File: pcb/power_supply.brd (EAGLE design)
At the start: 57.3 x 66.4 mm, 53 parts, among them CON1 +, CON2 +, CON3 +, CON4 +, CON5 +, CON6 +, CON7 +, CON8 +, IC1 AP1507-D5-13, P1 2k, Q1 DIODES_FMMT493ATADIODES_FMMT4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, Q2 DIODES_FMMT493ATADIODES_FMMT4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, Q3 DIODES_FMMT493ATADIODES_FMMT4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, Q4 DIODES_FMMT493ATADIODES_FMMT4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, Q5 DIODES_FMMT493ATADIODES_FMMT4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, Q6 DIODES_FMMT493ATADIODES_FMMT4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, Q7 DIODES_FMMT493ATADIODES_FMMT4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, Q8 DIODES_FMMT493ATADIODES_FMMT4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, U1 LM1085IT-ADJ

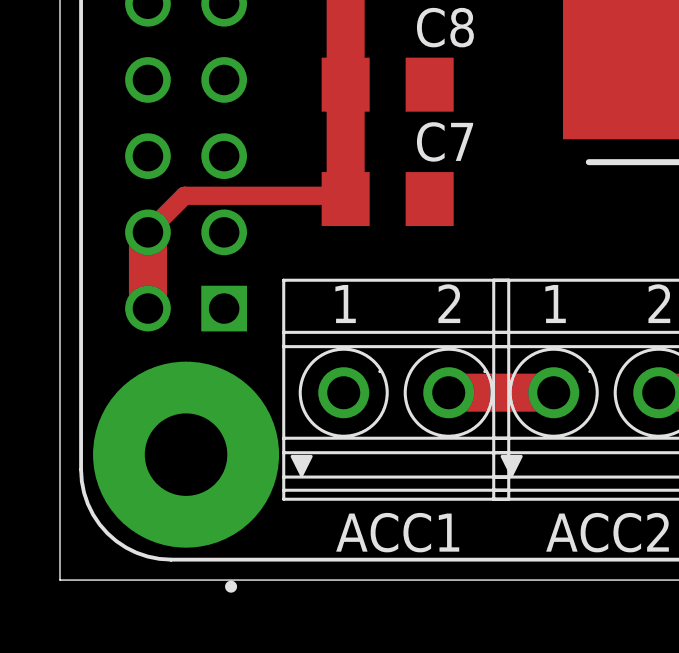
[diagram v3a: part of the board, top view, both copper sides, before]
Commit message: pcb - better supply route
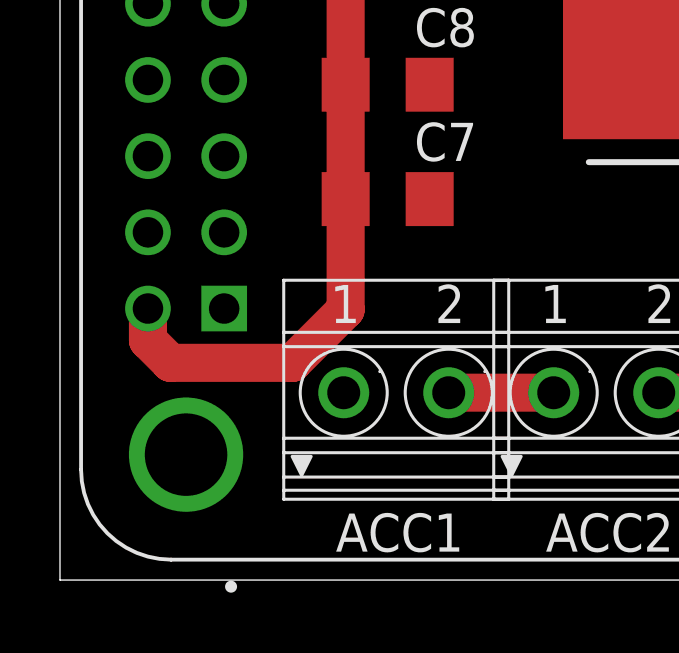
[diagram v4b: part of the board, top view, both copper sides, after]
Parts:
- RASPBERRY: device RASPBERRY_PI_3_MODEL_B_:MODULE_RASPBERRY_PI_3_MODEL_B+ -> RASPBERRY_PI_3_MODEL_B_NoScrew:MODULE_RASPBERRY_PI_3_MODEL_B+
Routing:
- net RASP_SUPPLY: track 34.5 -> 37.2 mm
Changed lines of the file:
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@@
 <attribute name="VALUE" x="18.796" y="48.641" size="1.27" layer="27"/>
 </element>
-<element name="RASPBERRY" library="RASPBERRY_PI_3_MODEL_B_" package="MODULE_RASPBERRY_PI_3_MODEL_B+" value="RASPBERRY_PI_3_MODEL_B+" x="29.21" y="44.45" smashed="yes" rot="R90">
+<element name="RASPBERRY" library="RASPBERRY_PI_3_MODEL_B_NoScrew" package="MODULE_RASPBERRY_PI_3_MODEL_B+" value="RASPBERRY_PI_3_MODEL_B+" x="29.21" y="44.45" smashed="yes" rot="R90">
 <attribute name="AVAILABILITY" value="In Stock" x="60.96" y="102.87" size="1.778" layer="27" rot="R90" display="off"/>
 <attribute name="DESCRIPTION" value=" RASPBERRY PI 3 MOD B+ BCM2837B0 " x="60.96" y="102.87" size="1.778" layer="27" rot="R90" display="off"/>
@@
 <contactref element="RASPBERRY" pad="1"/>
 <contactref element="RASPBERRY" pad="17"/>
-<wire x1="5.98" y1="30.64" x2="5.98" y2="10.32" width="0" layer="19" extent="1-1"/>
+<wire x1="5.98" y1="10.32" x2="5.98" y2="30.64" width="0" layer="19" extent="1-1"/>
 </signal>
 <signal name="GND">
@@
 <contactref element="Q8" pad="2"/>
 <contactref element="ACC1" pad="1"/>
-<wire x1="26.35" y1="27.94" x2="53.71" y2="63.45" width="0" layer="19" extent="1-1"/>
-<wire x1="34.42" y1="20.32" x2="26.35" y2="27.94" width="0" layer="19" extent="1-1"/>
+<wire x1="43.45" y1="58.74" x2="53.71" y2="63.45" width="0" layer="19" extent="1-1"/>
+<wire x1="43.45" y1="52.39" x2="43.45" y2="58.74" width="0" layer="19" extent="1-1"/>
+<wire x1="43.45" y1="46.04" x2="43.45" y2="52.39" width="0" layer="19" extent="1-1"/>
+<wire x1="43.45" y1="39.69" x2="43.45" y2="46.04" width="0" layer="19" extent="1-1"/>
+<wire x1="43.45" y1="33.34" x2="43.45" y2="39.69" width="0" layer="19" extent="1-1"/>
+<wire x1="43.45" y1="26.99" x2="43.45" y2="33.34" width="0" layer="19" extent="1-1"/>
+<wire x1="39.37" y1="22.86" x2="43.45" y2="26.99" width="0" layer="19" extent="1-1"/>
+<wire x1="34.42" y1="20.32" x2="39.37" y2="22.86" width="0" layer="19" extent="1-1"/>
 <wire x1="34.42" y1="16.51" x2="34.42" y2="20.32" width="0" layer="19" extent="1-1"/>
-<wire x1="32.854" y1="8.89" x2="34.42" y2="16.51" width="0" layer="19" extent="1-1"/>
-<wire x1="32.854" y1="12.7" x2="32.854" y2="8.89" width="0" layer="19" extent="1-1"/>
-<wire x1="39.37" y1="22.86" x2="32.854" y2="12.7" width="0" layer="19" extent="1-1"/>
-<wire x1="20.14" y1="19.05" x2="32.854" y2="8.89" width="0" layer="19" extent="1-1"/>
-<wire x1="26.885" y1="19.05" x2="20.14" y2="19.05" width="0" layer="19" extent="1-1"/>
-<wire x1="26.885" y1="21.59" x2="26.885" y2="19.05" width="0" layer="19" extent="1-1"/>
-<wire x1="5.98" y1="40.8" x2="26.885" y2="21.59" width="0" layer="19" extent="1-1"/>
+<wire x1="32.854" y1="12.7" x2="34.42" y2="16.51" width="0" layer="19" extent="1-1"/>
+<wire x1="32.854" y1="8.89" x2="32.854" y2="12.7" width="0" layer="19" extent="1-1"/>
+<wire x1="33.02" y1="25.72" x2="34.42" y2="20.32" width="0" layer="19" extent="1-1"/>
+<wire x1="33.02" y1="32.07" x2="33.02" y2="25.72" width="0" layer="19" extent="1-1"/>
+<wire x1="33.02" y1="38.42" x2="33.02" y2="32.07" width="0" layer="19" extent="1-1"/>
+<wire x1="33.02" y1="44.77" x2="33.02" y2="38.42" width="0" layer="19" extent="1-1"/>
+<wire x1="33.02" y1="51.12" x2="33.02" y2="44.77" width="0" layer="19" extent="1-1"/>
+<wire x1="33.02" y1="57.47" x2="33.02" y2="51.12" width="0" layer="19" extent="1-1"/>
+<wire x1="26.35" y1="27.94" x2="33.02" y2="25.72" width="0" layer="19" extent="1-1"/>
+<wire x1="26.885" y1="21.59" x2="26.35" y2="27.94" width="0" layer="19" extent="1-1"/>
+<wire x1="26.885" y1="19.05" x2="26.885" y2="21.59" width="0" layer="19" extent="1-1"/>
+<wire x1="20.14" y1="19.05" x2="26.885" y2="19.05" width="0" layer="19" extent="1-1"/>
+<wire x1="12.83" y1="17.78" x2="20.14" y2="19.05" width="0" layer="19" extent="1-1"/>
+<wire x1="12.83" y1="13.97" x2="12.83" y2="17.78" width="0" layer="19" extent="1-1"/>
+<wire x1="9.9657" y1="7.5138" x2="12.83" y2="13.97" width="0" layer="19" extent="1-1"/>
+<wire x1="4.71" y1="5.45" x2="9.9657" y2="7.5138" width="0" layer="19" extent="1-1"/>
+<wire x1="5.98" y1="20.48" x2="12.83" y2="17.78" width="0" layer="19" extent="1-1"/>
+<wire x1="3.44" y1="25.56" x2="5.98" y2="20.48" width="0" layer="19" extent="1-1"/>
+<wire x1="3.44" y1="15.4" x2="5.98" y2="20.48" width="0" layer="19" extent="1-1"/>
+<wire x1="25.67" y1="56.2" x2="33.02" y2="57.47" width="0" layer="19" extent="1-1"/>
+<wire x1="25.67" y1="49.85" x2="25.67" y2="56.2" width="0" layer="19" extent="1-1"/>
+<wire x1="3.44" y1="33.18" x2="3.44" y2="25.56" width="0" layer="19" extent="1-1"/>
+<wire x1="38.7985" y1="3.8471" x2="32.854" y2="8.89" width="0" layer="19" extent="1-1"/>
+<wire x1="25.4" y1="40.3" x2="33.02" y2="38.42" width="0" layer="19" extent="1-1"/>
+<wire x1="5.98" y1="40.8" x2="3.44" y2="33.18" width="0" layer="19" extent="1-1"/>
 <wire x1="3.44" y1="45.88" x2="5.98" y2="40.8" width="0" layer="19" extent="1-1"/>
 <wire x1="3.44" y1="50.96" x2="3.44" y2="45.88" width="0" layer="19" extent="1-1"/>
 <wire x1="5.98" y1="58.58" x2="3.44" y2="50.96" width="0" layer="19" extent="1-1"/>
 <wire x1="4.71" y1="63.45" x2="5.98" y2="58.58" width="0" layer="19" extent="1-1"/>
-<wire x1="3.44" y1="33.18" x2="5.98" y2="40.8" width="0" layer="19" extent="1-1"/>
-<wire x1="3.44" y1="25.56" x2="3.44" y2="33.18" width="0" layer="19" extent="1-1"/>
-<wire x1="5.98" y1="20.48" x2="3.44" y2="25.56" width="0" layer="19" extent="1-1"/>
-<wire x1="25.4" y1="40.3" x2="5.98" y2="20.48" width="0" layer="19" extent="1-1"/>
-<wire x1="3.44" y1="15.4" x2="5.98" y2="20.48" width="0" layer="19" extent="1-1"/>
-<wire x1="12.83" y1="13.97" x2="3.44" y2="15.4" width="0" layer="19" extent="1-1"/>
-<wire x1="12.83" y1="17.78" x2="12.83" y2="13.97" width="0" layer="19" extent="1-1"/>
-<wire x1="9.9657" y1="7.5138" x2="12.83" y2="13.97" width="0" layer="19" extent="1-1"/>
-<wire x1="4.71" y1="5.45" x2="9.9657" y2="7.5138" width="0" layer="19" extent="1-1"/>
-<wire x1="53.595" y1="11.43" x2="39.37" y2="22.86" width="0" layer="19" extent="1-1"/>
-<wire x1="53.71" y1="5.45" x2="53.595" y2="11.43" width="0" layer="19" extent="1-1"/>
-<wire x1="38.7985" y1="3.8471" x2="53.595" y2="11.43" width="0" layer="19" extent="1-1"/>
-<wire x1="33.02" y1="25.72" x2="4.71" y2="63.45" width="0" layer="19" extent="1-1"/>
-<wire x1="33.02" y1="32.07" x2="33.02" y2="25.72" width="0" layer="19" extent="1-1"/>
-<wire x1="33.02" y1="38.42" x2="33.02" y2="32.07" width="0" layer="19" extent="1-1"/>
-<wire x1="33.02" y1="44.77" x2="33.02" y2="38.42" width="0" layer="19" extent="1-1"/>
-<wire x1="43.45" y1="26.99" x2="33.02" y2="44.77" width="0" layer="19" extent="1-1"/>
-<wire x1="43.45" y1="33.34" x2="43.45" y2="26.99" width="0" layer="19" extent="1-1"/>
-<wire x1="43.45" y1="39.69" x2="43.45" y2="33.34" width="0" layer="19" extent="1-1"/>
-<wire x1="43.45" y1="46.04" x2="43.45" y2="39.69" width="0" layer="19" extent="1-1"/>
-<wire x1="25.67" y1="49.85" x2="43.45" y2="46.04" width="0" layer="19" extent="1-1"/>
-<wire x1="43.45" y1="52.39" x2="25.67" y2="49.85" width="0" layer="19" extent="1-1"/>
-<wire x1="25.67" y1="56.2" x2="43.45" y2="52.39" width="0" layer="19" extent="1-1"/>
-<wire x1="43.45" y1="58.74" x2="25.67" y2="56.2" width="0" layer="19" extent="1-1"/>
-<wire x1="15.24" y1="48.58" x2="25.67" y2="49.85" width="0" layer="19" extent="1-1"/>
-<wire x1="33.02" y1="51.12" x2="25.67" y2="56.2" width="0" layer="19" extent="1-1"/>
-<wire x1="33.02" y1="57.47" x2="43.45" y2="58.74" width="0" layer="19" extent="1-1"/>
+<wire x1="15.24" y1="54.93" x2="5.98" y2="58.58" width="0" layer="19" extent="1-1"/>
+<wire x1="15.24" y1="48.58" x2="15.24" y2="54.93" width="0" layer="19" extent="1-1"/>
+<wire x1="53.71" y1="5.45" x2="38.7985" y2="3.8471" width="0" layer="19" extent="1-1"/>
+<wire x1="53.595" y1="11.43" x2="53.71" y2="5.45" width="0" layer="19" extent="1-1"/>
 </signal>
 <signal name="BAT">
@@
 <wire x1="19.2608" y1="57.2592" x2="19.37" y2="57.15" width="0.6096" layer="1"/>
 <wire x1="4.6592" y1="57.2592" x2="19.2608" y2="57.2592" width="0.6096" layer="1"/>
-<wire x1="15.24" y1="56.83" x2="19.37" y2="57.15" width="0" layer="19" extent="1-1"/>
+<wire x1="19.37" y1="57.15" x2="15.56" y2="57.15" width="0" layer="19" extent="1-1"/>
 </signal>
 <signal name="N$27">
@@
 <wire x1="10.03" y1="37.55" x2="10.03" y2="13.97" width="1.27" layer="1"/>
 <wire x1="10.03" y1="13.97" x2="10.03" y2="14.0792" width="0.6096" layer="1"/>
-<wire x1="10.03" y1="14.0792" x2="4.6592" y2="14.0792" width="0.6096" layer="1"/>
-<wire x1="4.6592" y1="14.0792" x2="3.44" y2="12.86" width="0.6096" layer="1"/>
 <wire x1="3.80941875" y1="10.32" x2="3.44" y2="10.32" width="0.6096" layer="1"/>
-<wire x1="3.44" y1="12.86" x2="3.44" y2="10.32" width="1.27" layer="1"/>
+<wire x1="3.44" y1="10.32" x2="3.44" y2="9.26" width="1.27" layer="1"/>
+<wire x1="4.191" y1="8.509" x2="8.255" y2="8.509" width="1.27" layer="1"/>
+<wire x1="8.255" y1="8.509" x2="10.03" y2="10.284" width="1.27" layer="1"/>
+<wire x1="10.03" y1="10.284" x2="10.03" y2="13.97" width="1.27" layer="1"/>
+<wire x1="3.44" y1="9.26" x2="4.191" y2="8.509" width="1.27" layer="1"/>
 <wire x1="10.58" y1="38.1" x2="10.48" y2="27.94" width="0" layer="19" extent="1-1"/>
-<wire x1="10.03" y1="17.78" x2="10.03" y2="13.97" width="0" layer="19" extent="1-1"/>
+<wire x1="3.44" y1="12.86" x2="3.44" y2="10.32" width="0" layer="19" extent="1-1"/>
+<wire x1="10.03" y1="17.78" x2="10.03" y2="14.0792" width="0" layer="19" extent="1-1"/>
 </signal>
 <signal name="N$32">
